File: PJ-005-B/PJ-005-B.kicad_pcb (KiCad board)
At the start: 2 copper layers, 54 parts, among them J1 Conn_01x02_Pin, U1 MIC29302WU-TR, U10 B65821C1008T1, U2 MIC29302WU-TR, U3 MIC29302WU-TR, U4 MIC5365-2.5YC5-TR, U5 LM337IMP/NOPB, U6 LM7171AIMX/NOPB, U7 LM7171AIMX/NOPB, U8 LT1210CR-PBF, U9 LT1210CR-PBF

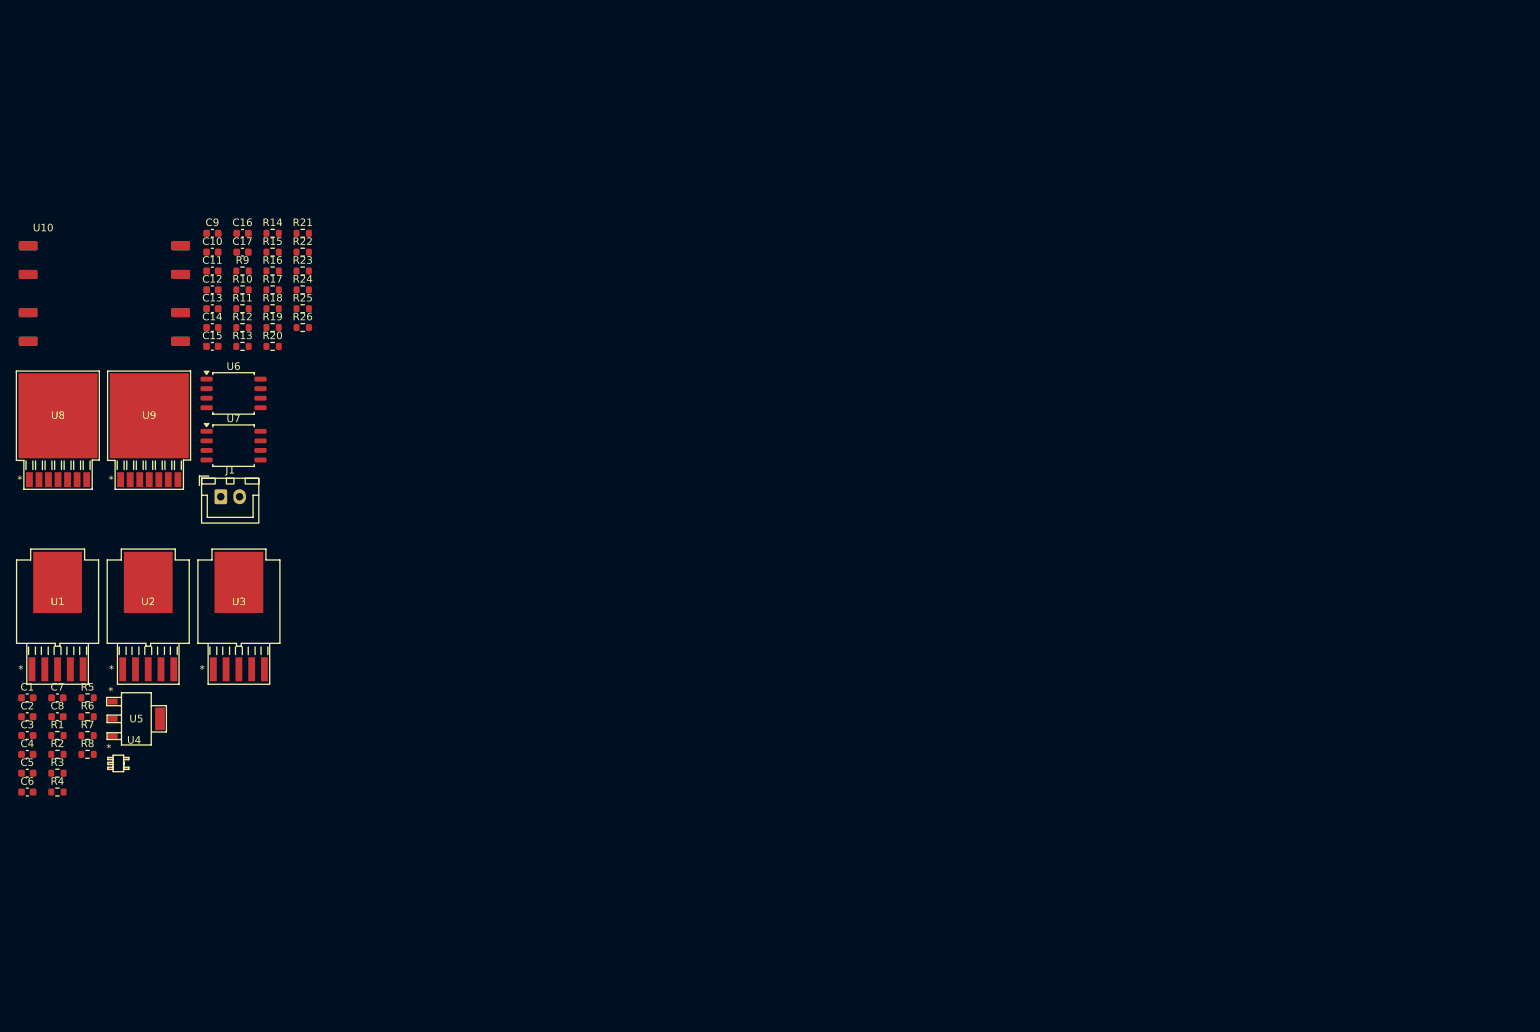
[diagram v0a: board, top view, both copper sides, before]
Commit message: -- Receive stage with charge amp-->inverting amp-->BPF-->inverting amp-->buffer-->PGA-->buffer -- Transmit stage with push pull mosfet -- TTL to RS485 converter -- LDOs 12V to 9V, 9V to 6V, 6V to 5V, 5V to 2.5V and -5V to -2.5V
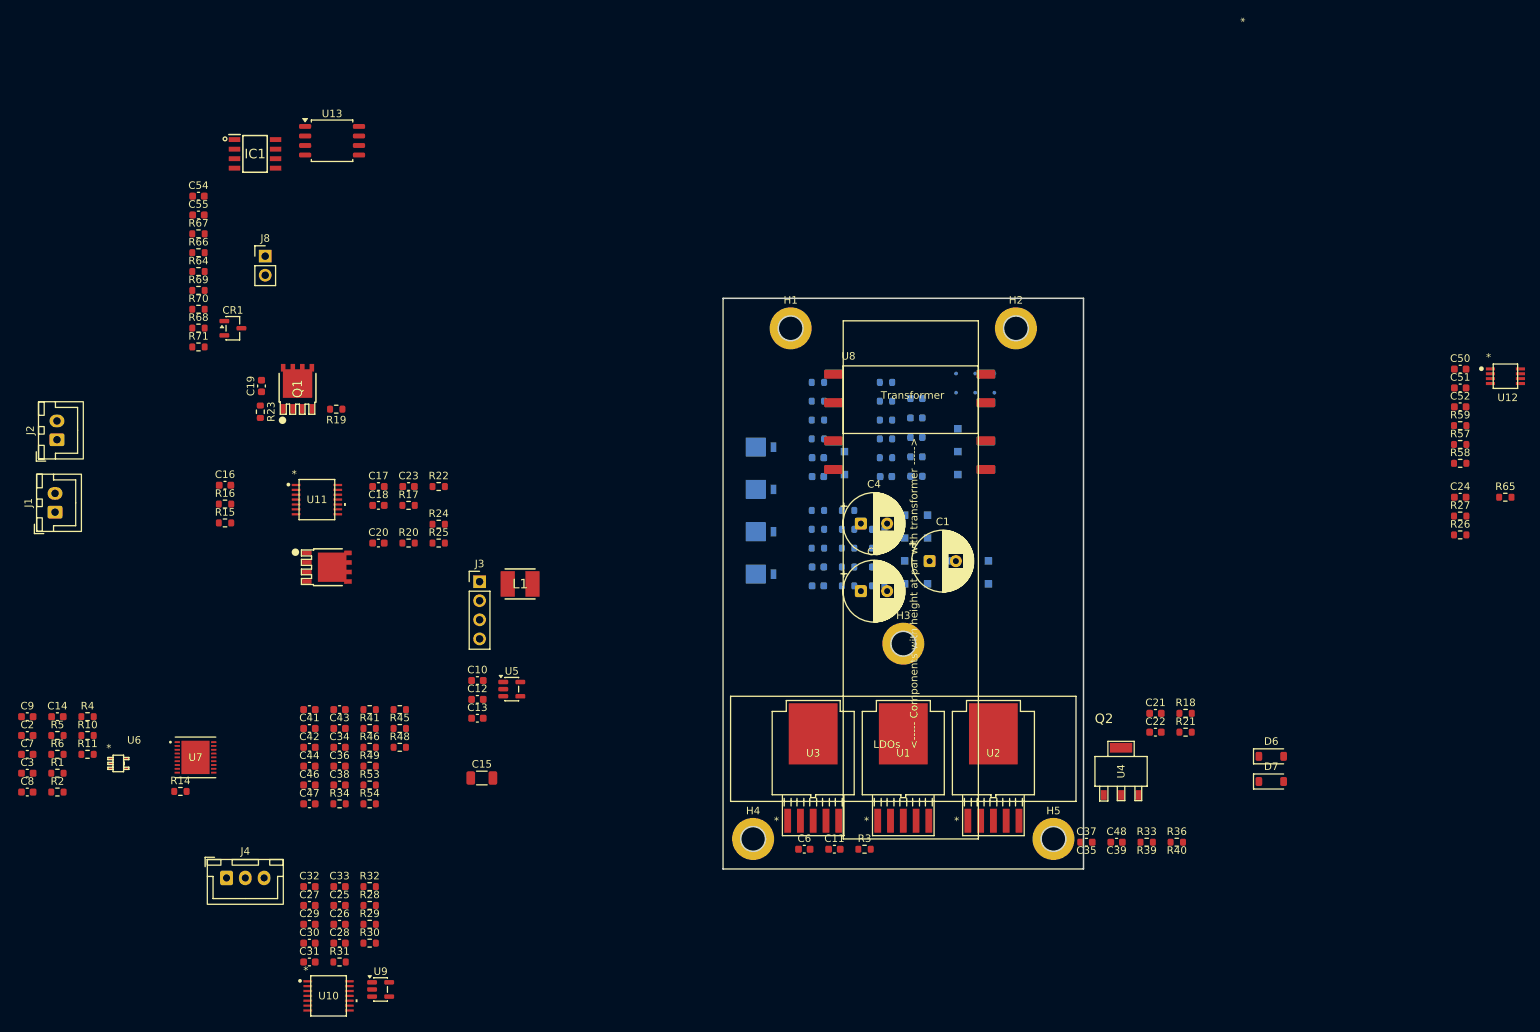
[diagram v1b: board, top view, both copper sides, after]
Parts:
- removed the C11 at (74.0, 58.4)
- removed the C14 at (74.0, 65.9)
- removed the C9 at (74.0, 53.3)
- removed the R10 at (78.0, 60.9)
- removed the R11 at (78.0, 63.4)
- removed the U6 at (76.8, 74.7)
- added C1: 1000uF,16V, Capacitor_THT:CP_Radial_D8.0mm_P3.50mm, F.Cu at (169.5, 97.0)
- added C18: 100nF,25V, XaltenFootprints:C0603, F.Cu at (96.1, 89.6)
- added C19: 3.9nF,25V, XaltenFootprints:C0603, F.Cu at (80.5, 73.7)
- added C20: 3.9nF,25V, XaltenFootprints:C0603, F.Cu at (96.1, 94.6)
- added C21: 10nF,200V, XaltenFootprints:C0603, F.Cu at (199.6, 117.3)
- added C22: 22nF,200V, XaltenFootprints:C0603, F.Cu at (199.6, 119.8)
- added C23: 22nF,200V, XaltenFootprints:C0603, F.Cu at (100.1, 87.1)
- added C24: 10nF,200V, XaltenFootprints:C0603, F.Cu at (240.2, 88.5)
- added C25: 2.2uF,25V, XaltenFootprints:C0603, F.Cu at (90.9, 142.9)
- added C26: 100nF,25V, XaltenFootprints:C0603, F.Cu at (90.9, 145.4)
- added C27: 1nF,25V, XaltenFootprints:C0603, F.Cu at (86.9, 142.9)
- added C28: 100pF,25V, XaltenFootprints:C0603, F.Cu at (90.9, 147.9)
- added C29: 100nF,25V, XaltenFootprints:C0603, F.Cu at (86.9, 145.4)
- added C30: 2.2uF,25V, XaltenFootprints:C0603, F.Cu at (86.9, 147.9)
- added C31: 100nF,25V, XaltenFootprints:C0603, F.Cu at (86.9, 150.4)
- added C32: 2pF,25V, XaltenFootprints:C0603, F.Cu at (86.9, 140.3)
- added C33: 100pF,25V, XaltenFootprints:C0603, F.Cu at (90.9, 140.3)
- added C34: 2.2uF,25V, XaltenFootprints:C0603, F.Cu at (90.9, 121.8)
- added C35: 121pF,25V, XaltenFootprints:C0603, F.Cu at (86.9, 116.8)
- added C36: 100nF,25V, XaltenFootprints:C0603, F.Cu at (90.9, 124.3)
- added C37: 100pF,25V, XaltenFootprints:C0603, F.Cu at (190.4, 134.4)
- added C38: 100pF,25V, XaltenFootprints:C0603, F.Cu at (90.9, 126.8)
- added C39: 100nF,25V, XaltenFootprints:C0603, F.Cu at (90.9, 116.8)
- added C4: 470uF,25V, Capacitor_THT:CP_Radial_D8.0mm_P3.50mm, F.Cu at (160.3, 92.0)
- added C40: 2pF,25V, XaltenFootprints:C0603, B.Cu at (154.6, 100.3)
- added C41: 715pF,25V, XaltenFootprints:C0603, F.Cu at (86.9, 119.3)
- added C42: 100pF,25V, XaltenFootprints:C0603, F.Cu at (86.9, 121.8)
- added C43: 100nF,25V, XaltenFootprints:C0603, F.Cu at (90.9, 119.3)
- added C44: 1.21nF,25V, XaltenFootprints:C0603, F.Cu at (86.9, 124.3)
- added C45: 2pF,25V, XaltenFootprints:C0603, B.Cu at (154.6, 97.8)
- added C46: 1nF,25V, XaltenFootprints:C0603, F.Cu at (86.9, 126.8)
- added C47: 3.16nF,25V, XaltenFootprints:C0603, F.Cu at (86.9, 129.3)
- added C48: 2.26nF,25V, XaltenFootprints:C0603, F.Cu at (194.4, 134.4)
- added C49: 1uF,16V, XaltenFootprints:C0603, B.Cu at (154.6, 85.7)
- added C5: 470uF,25V, Capacitor_THT:CP_Radial_D8.0mm_P3.50mm, F.Cu at (160.3, 101.0)
- added C50: 2.2uF,25V, XaltenFootprints:C0603, F.Cu at (240.2, 71.4)
- added C51: 100nF,25V, XaltenFootprints:C0603, F.Cu at (240.2, 73.9)
- added C52: 100pF,25V, XaltenFootprints:C0603, F.Cu at (240.2, 76.5)
- added C53: 2pF,25V, XaltenFootprints:C0603, B.Cu at (154.6, 83.2)
- added C54: 2.2uF,25V, XaltenFootprints:C0603, F.Cu at (72.1, 48.4)
- added C55: 100nF,25V, XaltenFootprints:C0603, F.Cu at (72.1, 50.9)
- added C56: 2.2uF,25V, XaltenFootprints:C0603, B.Cu at (163.7, 85.7)
- added CR1: SM712-02HTG, XaltenFootprints:SOT-23-3, F.Cu at (76.7, 66.0)
- added D1: RED, LED_SMD:LED_0603_1608Metric, B.Cu at (167.7, 85.7)
- added D10: AU1PMHM3_84A, Echosounder Transceiver FP:AU1PMHM384A, B.Cu at (147.0, 87.4)
- added D11: AU1PMHM3_84A, Echosounder Transceiver FP:AU1PMHM384A, B.Cu at (147.0, 81.8)
- added D2: RED, LED_SMD:LED_0603_1608Metric, B.Cu at (167.7, 83.1)
- added D3: RED, LED_SMD:LED_0603_1608Metric, B.Cu at (167.7, 80.5)
- added D4: GREEN, LED_SMD:LED_0603_1608Metric, B.Cu at (167.7, 77.9)
- added D5: YELLOW, LED_SMD:LED_0603_1608Metric, B.Cu at (167.7, 75.3)
- added D6: 1N4148W, XaltenFootprints:SOD-123, F.Cu at (215.0, 123.0)
- added D7: 1N4148W, XaltenFootprints:SOD-123, F.Cu at (215.0, 126.3)
- added D8: AU1PMHM3_84A, Echosounder Transceiver FP:AU1PMHM384A, B.Cu at (147.0, 98.7)
- added D9: AU1PMHM3_84A, Echosounder Transceiver FP:AU1PMHM384A, B.Cu at (147.0, 93.1)
- added FID1: Fiducial, Fiducial:Fiducial_0.5mm_Mask1mm, B.Cu at (173.0, 74.6)
- added FID2: Fiducial, Fiducial:Fiducial_0.5mm_Mask1mm, B.Cu at (173.0, 72.0)
- added FID3: Fiducial, Fiducial:Fiducial_0.5mm_Mask1mm, B.Cu at (175.6, 74.6)
- added FID4: Fiducial, Fiducial:Fiducial_0.5mm_Mask1mm, B.Cu at (175.6, 72.0)
- added FID5: Fiducial, Fiducial:Fiducial_0.5mm_Mask1mm, B.Cu at (178.1, 74.6)
- added FID6: Fiducial, Fiducial:Fiducial_0.5mm_Mask1mm, B.Cu at (178.1, 72.0)
- added H1: MountingHole_Pad, MountingHole:MountingHole_3.2mm_M3_DIN965_Pad, F.Cu at (151.0, 66.0)
- added H2: MountingHole_Pad, MountingHole:MountingHole_3.2mm_M3_DIN965_Pad, F.Cu at (181.0, 66.0)
- added H3: MountingHole_Pad, MountingHole:MountingHole_3.2mm_M3_DIN965_Pad, F.Cu at (166.0, 108.0)
- added H4: MountingHole_Pad, MountingHole:MountingHole_3.2mm_M3_DIN965_Pad, F.Cu at (146.0, 134.0)
- added H5: MountingHole_Pad, MountingHole:MountingHole_3.2mm_M3_DIN965_Pad, F.Cu at (186.0, 134.0)
- added IC1: 2EDN8534FXTMA1, Echosounder Transceiver FP:SOIC127P602X173-8N, F.Cu at (79.7, 42.8)
- added J2: 2 Pin JST XH, Connector_JST:JST_XH_B2B-XH-A_1x02_P2.50mm_Vertical, F.Cu at (53.3, 80.8)
- added J3: Pin Header 4 Pin, Connector_PinHeader_2.54mm:PinHeader_1x04_P2.54mm_Vertical, F.Cu at (109.6, 99.7)
- added J4: 3 Pin JST XH, Connector_JST:JST_XH_B3B-XH-A_1x03_P2.50mm_Vertical, F.Cu at (75.9, 139.2)
- added J8: Pin Header 2 Pin, Connector_PinHeader_2.54mm:PinHeader_1x02_P2.54mm_Vertical, F.Cu at (81.0, 56.4)
- added L1: 33uH,840mA, Echosounder Transceiver FP:INDPM4040X300N, F.Cu at (115.0, 100.0)
- added Q1: SIR622DP-T1-RE3, Echosounder Transceiver FP:SIR622DPT1RE3, F.Cu at (85.3, 74.0)
- added Q2: SIR622DP-T1-RE3, Echosounder Transceiver FP:SIR622DPT1RE3, F.Cu at (89.2, 97.8)
- added R27: 100K,1%, XaltenFootprints:R0603, F.Cu at (240.2, 91.0)
- added R28: 33R,1%, XaltenFootprints:R0603, F.Cu at (94.9, 142.9)
- added R29: 3K3,1%, XaltenFootprints:R0603, F.Cu at (94.9, 145.4)
- added R30: 0R, XaltenFootprints:R0603, F.Cu at (94.9, 147.9)
- added R31: 1K,1%, XaltenFootprints:R0603, F.Cu at (90.9, 150.4)
- added R32: 3K3,1%, XaltenFootprints:R0603, F.Cu at (94.9, 140.3)
- added R33: 8K06,0.1%, XaltenFootprints:R0603, F.Cu at (198.4, 134.4)
- added R34: 11K5,1%, XaltenFootprints:R0603, F.Cu at (90.9, 129.3)
- added R35: 0R, XaltenFootprints:R0603, B.Cu at (154.6, 95.3)
- added R36: 1K,1%, XaltenFootprints:R0603, F.Cu at (202.4, 134.4)
- added R37: 0R, XaltenFootprints:R0603, B.Cu at (154.6, 92.8)
- added R38: 0R, XaltenFootprints:R0603, B.Cu at (154.6, 90.3)
- added R39: 3K16,0.1%, XaltenFootprints:R0603, F.Cu at (94.9, 116.8)
- added R40: 10K,1%, XaltenFootprints:R0603, F.Cu at (98.9, 116.8)
- added R41: 4K99,0.1%, XaltenFootprints:R0603, F.Cu at (94.9, 119.3)
- added R42: 0R, XaltenFootprints:R0603, B.Cu at (158.6, 100.3)
- added R43: 0R, XaltenFootprints:R0603, B.Cu at (158.6, 97.8)
- added R44: 0R, XaltenFootprints:R0603, B.Cu at (158.6, 95.3)
- added R45: 1K,1%, XaltenFootprints:R0603, F.Cu at (98.9, 119.3)
- added R46: 2K26,0.1%, XaltenFootprints:R0603, F.Cu at (94.9, 121.8)
- added R47: 0R, XaltenFootprints:R0603, B.Cu at (158.6, 92.8)
- added R48: 1K,1%, XaltenFootprints:R0603, F.Cu at (98.9, 121.8)
- added R49: 2K67,0.1%, XaltenFootprints:R0603, F.Cu at (94.9, 124.3)
- added R50: 0R, XaltenFootprints:R0603, B.Cu at (158.6, 90.3)
- added R51: 0R, XaltenFootprints:R0603, B.Cu at (162.7, 100.3)
- added R52: 0R, XaltenFootprints:R0603, B.Cu at (162.7, 97.8)
- added R53: 2K67,0.1%, XaltenFootprints:R0603, F.Cu at (94.9, 126.8)
- added R54: 2K67,0.1%, XaltenFootprints:R0603, F.Cu at (94.9, 129.3)
- added R55: 0R, XaltenFootprints:R0603, B.Cu at (162.7, 95.3)
- added R56: 0R, XaltenFootprints:R0603, B.Cu at (162.7, 92.8)
- added R57: 10R,1%, XaltenFootprints:R0603, F.Cu at (240.2, 81.5)
- added R58: 10R,1%, XaltenFootprints:R0603, F.Cu at (240.2, 84.0)
- added R59: 4K7,1%, XaltenFootprints:R0603, F.Cu at (240.2, 79.0)
- added R60: 0R, XaltenFootprints:R0603, B.Cu at (154.6, 80.7)
- added R61: 0R, XaltenFootprints:R0603, B.Cu at (154.6, 78.2)
- added R62: 1K,1%, XaltenFootprints:R0603, B.Cu at (154.6, 75.7)
- added R63: 1K,1%, XaltenFootprints:R0603, B.Cu at (154.6, 73.2)
- added R64: 1K,1%, XaltenFootprints:R0603, F.Cu at (72.1, 58.4)
- added R65: 1K,1%, XaltenFootprints:R0603, F.Cu at (246.2, 88.5)
- added R66: 1K,1%, XaltenFootprints:R0603, F.Cu at (72.1, 55.9)
- added R67: 1K,1%, XaltenFootprints:R0603, F.Cu at (72.1, 53.4)
- added R68: 120R,1%, XaltenFootprints:R0603, F.Cu at (72.1, 66.0)
- added R69: 680R,1%, XaltenFootprints:R0603, F.Cu at (72.1, 60.9)
- added R7: 3K3,1%, XaltenFootprints:R0603, B.Cu at (163.7, 83.2)
- added R70: 680R,1%, XaltenFootprints:R0603, F.Cu at (72.1, 63.5)
- added R71: 120R,1%, XaltenFootprints:R0603, F.Cu at (72.1, 68.5)
- added R8: 4K7,1%, XaltenFootprints:R0603, B.Cu at (163.7, 80.7)
- added TP1: TestPoint, TestPoint:TestPoint_Pad_1.0x1.0mm, B.Cu at (173.3, 85.5)
- added TP10: TestPoint, TestPoint:TestPoint_Pad_1.0x1.0mm, B.Cu at (169.2, 100.0)
- added TP11: TestPoint, TestPoint:TestPoint_Pad_1.0x1.0mm, B.Cu at (169.2, 97.0)
- added TP12: TestPoint, TestPoint:TestPoint_Pad_1.0x1.0mm, B.Cu at (169.2, 93.9)
- added TP13: TestPoint, TestPoint:TestPoint_Pad_1.0x1.0mm, B.Cu at (169.2, 90.9)
- added TP14: TestPoint, TestPoint:TestPoint_Pad_1.0x1.0mm, B.Cu at (172.3, 100.0)
- added TP15: TestPoint, TestPoint:TestPoint_Pad_1.0x1.0mm, B.Cu at (172.3, 97.0)
- added TP16: TestPoint, TestPoint:TestPoint_Pad_1.0x1.0mm, B.Cu at (172.3, 93.9)
- added TP17: TestPoint, TestPoint:TestPoint_Pad_1.0x1.0mm, B.Cu at (158.2, 85.5)
- added TP18: TestPoint, TestPoint:TestPoint_Pad_1.0x1.0mm, B.Cu at (158.2, 82.4)
- added TP2: TestPoint, TestPoint:TestPoint_Pad_1.0x1.0mm, B.Cu at (173.3, 82.4)
- added TP3: TestPoint, TestPoint:TestPoint_Pad_1.0x1.0mm, B.Cu at (173.3, 79.4)
- added TP4: TestPoint, TestPoint:TestPoint_Pad_1.0x1.0mm, B.Cu at (177.3, 100.0)
- added TP5: TestPoint, TestPoint:TestPoint_Pad_1.0x1.0mm, B.Cu at (177.3, 97.0)
- added TP6: TestPoint, TestPoint:TestPoint_Pad_1.0x1.0mm, B.Cu at (166.2, 100.0)
- added TP7: TestPoint, TestPoint:TestPoint_Pad_1.0x1.0mm, B.Cu at (166.2, 97.0)
- added TP8: TestPoint, TestPoint:TestPoint_Pad_1.0x1.0mm, B.Cu at (166.2, 93.9)
- added TP9: TestPoint, TestPoint:TestPoint_Pad_1.0x1.0mm, B.Cu at (166.2, 90.9)
- added U11: AD8608ARUZ-REEL, Echosounder Transceiver FP:RU_14_ADI-L, F.Cu at (87.9, 88.8)
- added U12: MCP6S91-E/MS, Echosounder Transceiver FP:MSOP8, F.Cu at (246.2, 72.4)
- added U13: MAX485CSA+T, XaltenFootprints:SOIC-8-5.3x5.3x1.27, F.Cu at (89.9, 41.0)
- added U5: REF2033AIDDCR, XaltenFootprints:SOT-23-5, F.Cu at (113.9, 114.0)
- C10: value C -> 2.2uF,25V
- C13: value C -> 100pF,25V
- C15: value 100nF,25V -> 4.7uF,25V; footprint XaltenFootprints:C0603 -> XaltenFootprints:C1206
- C17: value 1uF,25V -> 100nF,25V
- J1: value Conn_01x02_Pin -> 2 Pin JST XH
- R12, R13: value 1K,1% -> 499R,1%; moved to B.Cu
- R14: value 1K,1% -> 0R
- R15: value 33K,1% -> 10K,1%
- R16, R17: value 576R,1% -> 10K,1%
- R18: value 1K,1% -> 10K,1%
- R19: value 1K5,1% -> 4R7,1%
- R20: value 1K5,1% -> 2R2,1%
- R21: value 1K,1% -> 4R7,1%
- R22: value 33K,1% -> 2R2,1%
- R23, R24: value 576R,1% -> 12R,1%
- R25: value R -> 330R,1%
- R26: value R -> 2R5,1%
- R9: value 1K,1% -> 10K,1%; moved to B.Cu
- U10: value B65821C1008T1 -> AD8608ARUZ-REEL; footprint Echosounder Transceiver FP:RM6 -> Echosounder Transceiver FP:RU_14_ADI-L
- U7: value LM7171AIMX/NOPB -> MD0105K6-G; footprint XaltenFootprints:SOIC-8-5.3x5.3x1.27 -> Echosounder Transceiver FP:DFN18
- U8: value LT1210CR-PBF -> B65821C1008T1; footprint Echosounder Transceiver FP:DDPAK-7 -> Echosounder Transceiver FP:RM6
- U9: value LT1210CR-PBF -> TLV365QDBVRQ1; footprint Echosounder Transceiver FP:DDPAK-7 -> XaltenFootprints:SOT-23-5
- moved R26 156.6 mm to (240.2, 93.5)
- moved R21 135.0 mm to (203.6, 119.8)
- moved R18 133.0 mm to (203.6, 117.3)
- moved U4 131.3 mm to (195.0, 125.0), turned to 90 degrees
- moved U10 107.6 mm to (89.5, 154.9)
- moved C11 105.4 mm to (156.8, 135.4)
- moved C6 105.4 mm to (152.8, 135.4)
- moved R3 105.4 mm to (160.8, 135.4)
- moved U8 103.4 mm to (156.7, 72.1)
- moved U3 102.6 mm to (154.0, 122.6)
- moved U1 102.6 mm to (166.0, 122.6)
- moved U2 102.5 mm to (178.0, 122.6)
- moved R9 88.0 mm to (163.7, 78.2)
- moved R12 86.3 mm to (163.7, 75.7)
- moved R13 85.8 mm to (163.7, 73.2)
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- renumbered C7 to C11, C8 to C14, C3 to C2, C5 to C3, C1 to C6, C4 to C7, C6 to C8, C2 to C9, R3 to R1, R7 to R10, R8 to R11, R4 to R2, R5 to R3, R6 to R4, R1 to R5, R2 to R6, U2 to U1, U3 to U2, U1 to U3, U5 to U4, U4 to U6
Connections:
- net /Power/6V renamed +6V
- C10 pad 1: Net-(U6--IN) -> +5V
- C10 pad 2: Net-(U6-OUT) -> TxD_N
- C11 pad 2: GND -> TxD_N
- C12 pad 1: Net-(J1-Pin_2) -> TxD_N
- C12 pad 2: Net-(C12-Pad2) -> +5V
- C13 pad 1: Net-(U7--IN) -> TxD_N
- C13 pad 2: Net-(U7-OUT) -> +5V
- C14 pad 2: GND -> TxD_N
- C15 pad 1: Net-(U8-COMP) -> +12V
- C15 pad 2: Net-(U8-OUT) -> TxD_N
- C16 pad 1: Net-(U9-COMP) -> TxD_N
- C16 pad 2: Net-(U9-OUT) -> +12V
- C17 pad 1: Net-(C17-Pad1) -> +12V
- C17 pad 2: Net-(C17-Pad2) -> TxD_N
- C2 pad 1: /Power/9V -> +9V
- C2 pad 2: GND -> TxD_N
- C3 pad 2: GND -> TxD_N
- C6 pad 1: /Power/12V -> +12V
- C6 pad 2: GND -> TxD_N
- C7 pad 2: GND -> TxD_N
- C8 pad 2: GND -> TxD_N
- C9 pad 1: /Power/9V -> +9V
- C9 pad 2: GND -> TxD_N
- J1 pad 1: GND -> TxD_N
- J1 pad 2: Net-(J1-Pin_2) -> +12V
- R11 pad 2: unconnected-(R8-Pad2) -> TxD_N
- R12 pad 1: Net-(R11-Pad2) -> -2V5
- R12 pad 2: Net-(U6-OUT) -> Net-(D4-K)
- R13 pad 1: GND -> +2V5
- R13 pad 2: Net-(U6--IN) -> Net-(D5-A)
- R14 pad 1: Net-(C11-Pad2) -> /Receiver/Charge Amp + Inverting Amp/AMP_OUT
- R14 pad 2: Net-(U8-+IN) -> /Receiver/Filter + Inverting Amp + Buffer/FILTER_IN
- R15 pad 1: GND -> /Transmit/EN_B
- R15 pad 2: Net-(U8-+IN) -> TxD_N
- R16 pad 1: Net-(U8--IN) -> /Transmit/EN_A
- R16 pad 2: Net-(U8-OUT) -> TxD_N
- R17 pad 1: GND -> TxD_N
- R17 pad 2: Net-(U8--IN) -> /Transmit/PWM_OUT_A
- R18 pad 1: Net-(C12-Pad2) -> /Transmit/PWM_OUT_B
- R18 pad 2: Net-(U7--IN) -> TxD_N
- R19 pad 1: Net-(U7--IN) -> /Transmit/PWM_OUT_A
- R19 pad 2: Net-(R19-Pad2) -> Net-(Q1-G)
- R2 pad 2: GND -> TxD_N
- R20 pad 1: Net-(R19-Pad2) -> Net-(D6-A)
- R20 pad 2: Net-(U7-OUT) -> Net-(Q1-G)
- R21 pad 1: Net-(C14-Pad2) -> /Transmit/PWM_OUT_B
- R21 pad 2: Net-(U9-+IN) -> Net-(Q2-G)
- R22 pad 1: GND -> Net-(D7-A)
- R22 pad 2: Net-(U9-+IN) -> Net-(Q2-G)
- R23 pad 1: Net-(U9--IN) -> Net-(C19-Pad1)
- R23 pad 2: Net-(U9-OUT) -> TxD_N
- R24 pad 1: GND -> TxD_N
- R24 pad 2: Net-(U9--IN) -> Net-(C20-Pad2)
- R25 pad 1: Net-(U8-OUT) -> TxD_N
- R25 pad 2: Net-(R25-Pad2) -> Net-(C21-Pad2)
- R26 pad 1: Net-(U9-OUT) -> Net-(D10-K)
- R26 pad 2: Net-(R26-Pad2) -> TxD_P
- R4 pad 2: GND -> TxD_N
- R5 pad 1: /Power/9V -> +9V
- R6 pad 2: GND -> TxD_N
- R9 pad 1: Net-(C9-Pad2) -> +9V
- U1 pad 1: /Power/9V -> +9V
- U1 pad 2: /Power/9V -> +9V
- U1 pad 3: GND -> TxD_N
- U1 pad 6: GND -> TxD_N
- U10 pad 1: Net-(R25-Pad2) -> /Receiver/Charge Amp + Inverting Amp/AMP_OUT
- U10 pad 2: Net-(C17-Pad2) -> Net-(U10A--INA)
- U10 pad 3: Net-(C17-Pad1) -> VREF
- U10 pad 4: Net-(R26-Pad2) -> +3.3V
- U10 pad 5: unconnected-(U10-Pad5) -> VREF
- U10 pad 6: unconnected-(U10-Pad6) -> Net-(U10B--INB)
- U10 pad 7: unconnected-(U10-Pad7) -> Net-(U10B-OUTB)
- U10 pad 8: unconnected-(U10-Pad8) -> Net-(U10C-OUTC)
- U2 pad 3: GND -> TxD_N
- U2 pad 6: GND -> TxD_N
- U3 pad 1: /Power/12V -> +12V
- U3 pad 2: /Power/12V -> +12V
- U3 pad 3: GND -> TxD_N
- U3 pad 4: /Power/9V -> +9V
- U3 pad 6: GND -> TxD_N
- U6 pad 2: GND -> TxD_N
- U7 pad 2: Net-(U7--IN) -> TxD_P
- U7 pad 3: GND -> unconnected-(U7-NC-Pad3)
- U7 pad 4: -12V -> unconnected-(U7-A2-Pad4)
- U7 pad 6: Net-(U7-OUT) -> unconnected-(U7-A3-Pad6)
- U7 pad 7: +12V -> unconnected-(U7-NC-Pad7)
- U8 pad 1: Net-(U8--IN) -> Net-(Q1-D)
- U8 pad 2: Net-(U8-+IN) -> +12V
- U8 pad 3: /Transmit/SD1 -> +12V
- U8 pad 4: +12V -> Net-(Q2-D)
- U8 pad 5: Net-(U8-COMP) -> TxD_N
- U8 pad 6: -12V -> unconnected-(U8-Pad6)
- U8 pad 7: Net-(U8-OUT) -> unconnected-(U8-Pad7)
- U8 pad 8: (no net) -> Net-(C21-Pad1)
- U9 pad 1: Net-(U9--IN) -> Net-(U9-VOUT)
- U9 pad 2: Net-(U9-+IN) -> -2V5
- U9 pad 3: /Transmit/SD2 -> TxD_N
- U9 pad 4: unconnected-(U9-V+-Pad4) -> Net-(U9--IN)
- U9 pad 5: Net-(U9-COMP) -> +2V5
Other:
- board outline added: 48 x 76 mm
- board text added: "<----- Components with height at par with transformer ----->"
- board text added: "Clearance on back side is 1.5mm for the area where the 3d print covers Refer the PDF file for more info"
- board text added: "LDOs"
- board text added: "Transformer"

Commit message: no message
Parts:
- moved C21 264.6 mm to (-49.6, 28.2)
- moved C22 264.6 mm to (-49.6, 30.7)
- moved C24 264.6 mm to (-9.01, -0.56)
- moved C50 264.6 mm to (-9.01, -17.6)
- moved C51 264.6 mm to (-9.01, -15.1)
- moved C52 264.6 mm to (-9.01, -12.6)
- moved D6 264.6 mm to (-34.2, 33.9)
- moved D7 264.6 mm to (-34.2, 37.3)
- moved R18 264.6 mm to (-45.6, 28.2)
- moved R21 264.6 mm to (-45.6, 30.7)
- moved R26 264.6 mm to (-9.01, 4.46)
- moved R27 264.6 mm to (-9.01, 1.95)
- moved R57 264.6 mm to (-9.01, -7.58)
- moved R58 264.6 mm to (-9.01, -5.07)
- moved R59 264.6 mm to (-9.01, -10.1)
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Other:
- board text added: "<----------------LDOs--------------->"
- board text added: "<--Transformer-->"
- board text removed: "LDOs"

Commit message: Transceiver After Review
-- Added bulk capacitors for -2.5V LDO
-- Added 0R for shorting RE and DE in TTL to RS485
-- Changed the snubber values in transformer primary to 2.2nF and 33R
-- Removed the 10nF and 100K in parallel with the transducer
-- Added 1000uF capacitor for transformer centre tap
-- Added 100pF decoupling capacitor for gate driver IC
--Changed secondary snubber values to 220nF and 680R
-- Changed LC inductor value to 100uH (transformer secondary)
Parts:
- removed J2: 2 Pin JST XH, Connector_JST:JST_XH_B2B-XH-A_1x02_P2.50mm_Vertical
- added C57: 100pF,25V, XaltenFootprints:C0603, F.Cu at (198.4, 105.5)
- added C58: 1000uF,35V, Capacitor_THT:CP_Radial_D8.0mm_P3.50mm, F.Cu at (199.6, 99.5)
- added C59: 4.7uF,25V, XaltenFootprints:C1206, F.Cu at (209.8, 95.2)
- added J5: Pin Header 3 Pin, Connector_PinHeader_2.54mm:PinHeader_1x03_P2.54mm_Vertical, F.Cu at (151.2, 92.6)
- added J6: Conn_01x02_Pin, Connector_JST:JST_XH_B2B-XH-A_1x02_P2.50mm_Vertical, F.Cu at (156.0, 101.3)
- added J7: Pin Header 4 Pin, Connector_PinHeader_2.54mm:PinHeader_1x04_P2.54mm_Vertical, F.Cu at (179.3, 102.8)
- added J9: Conn_01x02_Pin, Connector_PinHeader_2.54mm:PinHeader_1x02_P2.54mm_Vertical, F.Cu at (174.5, 98.8)
- C11, C16, C17, C18, C22, C23, C25, C26, C27, C28, C29, C3, C30, C31, C32, C33, C34, C35, C36, C38, C39, C41, C42, C43, C44, C46, C47, C50, C51, C52, C6, C7, C8, D6, D7, R1, R11, R14, R15, R16, R17, R18, R2, R20, R21, R22, R28, R29, R3, R30, R31, R32, R34, R39, R40, R41, R45, R46, R48, R49, R53, R54, R59, R6: moved to B.Cu
- C19: value 3.9nF,25V -> 2.2nF,50V
- C20: value 3.9nF,25V -> 2.2nF,50V; moved to B.Cu
- C21: value 10nF,200V -> 220pF,400V; moved to B.Cu
- C24: value 10nF,200V -> 4.7uF,25V; footprint XaltenFootprints:C0603 -> XaltenFootprints:C1206
- L1: value 33uH,840mA -> 100uH,840mA
- R23: value 12R,1% -> 33R,1%
- R24: value 12R,1% -> 33R,1%; moved to B.Cu
- R25: value 330R,1% -> 680R,1%,500mW; moved to B.Cu
- R27: value 100K,1% -> 0R
- R64, R66, R67: value 1K,1% -> 10K,1%
- R65: value 1K,1% -> 10K,1%; moved to B.Cu
- moved R27 241.4 mm to (210.2, 103.0)
- moved U8 239.0 mm to (176.5, 84.5), turned to 180 degrees
- moved C24 237.6 mm to (209.8, 91.9)
- moved C1 221.7 mm to (160.9, 92.7)
- moved U4 218.3 mm to (145.8, 123.6)
- moved C4 217.9 mm to (170.0, 92.2)
- moved C5 201.2 mm to (166.0, 100.3)
- moved U12 194.5 mm to (155.3, 96.4)
- moved C50 193.1 mm to (165.1, 65.9), turned to 90 degrees
- moved R26 190.1 mm to (171.0, 65.7), turned to 90 degrees
- moved C51 189.8 mm to (162.6, 65.9), turned to 90 degrees
- moved U3 188.5 mm to (154.9, 123.2)
- moved U2 187.9 mm to (177.6, 123.2)
- moved C52 186.5 mm to (160.1, 65.9), turned to 90 degrees
- moved R58 184.6 mm to (161.4, 65.7), turned to 90 degrees
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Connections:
- C1 pad 2: TxD_N -> GND
- C10 pad 2: TxD_N -> GND
- C11 pad 2: TxD_N -> GND
- C12 pad 1: TxD_N -> GND
- C13 pad 1: TxD_N -> GND
- C14 pad 2: TxD_N -> GND
- C15 pad 2: TxD_N -> GND
- C16 pad 1: TxD_N -> GND
- C17 pad 2: TxD_N -> GND
- C18 pad 2: TxD_N -> GND
- C2 pad 2: TxD_N -> GND
- C23 pad 2: TxD_N -> GND
- C24 pad 1: TxD_P -> GND
- C24 pad 2: TxD_N -> -5V
- C25 pad 2: TxD_N -> GND
- C26 pad 1: TxD_N -> GND
- C28 pad 1: TxD_N -> GND
- C3 pad 2: TxD_N -> GND
- C30 pad 2: TxD_N -> GND
- C31 pad 1: TxD_N -> GND
- C33 pad 1: TxD_N -> GND
- C34 pad 2: TxD_N -> GND
- C36 pad 1: TxD_N -> GND
- C37 pad 2: TxD_N -> GND
- C38 pad 1: TxD_N -> GND
- C4 pad 2: TxD_N -> GND
- C42 pad 2: TxD_N -> GND
- C5 pad 2: TxD_N -> GND
- C50 pad 1: TxD_N -> GND
- C51 pad 2: TxD_N -> GND
- C52 pad 2: TxD_N -> GND
- C54 pad 2: TxD_N -> GND
- C55 pad 2: TxD_N -> GND
- C56 pad 2: TxD_N -> GND
- C6 pad 2: TxD_N -> GND
- C7 pad 2: TxD_N -> GND
- C8 pad 2: TxD_N -> GND
- C9 pad 2: TxD_N -> GND
- CR1 pad 3: TxD_N -> GND
- D1 pad 1: TxD_N -> GND
- D2 pad 1: TxD_N -> GND
- D3 pad 1: TxD_N -> GND
- D4 pad 2: TxD_N -> GND
- D5 pad 1: TxD_N -> GND
- H1 pad 1: TxD_N -> GND
- H2 pad 1: TxD_N -> GND
- H3 pad 1: TxD_N -> GND
- H4 pad 1: TxD_N -> GND
- H5 pad 1: TxD_N -> GND
- IC1 pad 3: TxD_N -> GND
- J1 pad 1: TxD_N -> GND
- J4 pad 1: TxD_N -> GND
- J4 pad 2: TxD_N -> GND
- Q1 pad 2: TxD_N -> GND
- Q2 pad 2: TxD_N -> GND
- R11 pad 2: TxD_N -> GND
- R15 pad 2: TxD_N -> GND
- R16 pad 2: TxD_N -> GND
- R17 pad 1: TxD_N -> GND
- R18 pad 2: TxD_N -> GND
- R2 pad 2: TxD_N -> GND
- R23 pad 2: TxD_N -> GND
- R24 pad 1: TxD_N -> GND
- R25 pad 1: TxD_N -> GND
- R27 pad 1: TxD_P -> /TTL to RS485/RE
- R27 pad 2: TxD_N -> /TTL to RS485/DE
- R4 pad 2: TxD_N -> GND
- R6 pad 2: TxD_N -> GND
- R65 pad 1: +5V -> /TTL to RS485/RE
- R65 pad 2: /TTL to RS485/RE -> GND
- R66 pad 1: +5V -> /TTL to RS485/DE
- R66 pad 2: /TTL to RS485/DE -> GND
- R70 pad 2: TxD_N -> GND
- U1 pad 3: TxD_N -> GND
- U1 pad 6: TxD_N -> GND
- U10 pad 11: TxD_N -> GND
- U11 pad 11: TxD_N -> GND
- U12 pad 4: TxD_N -> GND
- U13 pad 5: TxD_N -> GND
- U2 pad 3: TxD_N -> GND
- U2 pad 6: TxD_N -> GND
- U3 pad 3: TxD_N -> GND
- U3 pad 6: TxD_N -> GND
- U5 pad 2: TxD_N -> GND
- U6 pad 2: TxD_N -> GND
- U7 pad 19: TxD_N -> GND
- U8 pad 5: TxD_N -> GND
- U9 pad 3: TxD_N -> GND
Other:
- outline, holes or cut-outs redrawn
